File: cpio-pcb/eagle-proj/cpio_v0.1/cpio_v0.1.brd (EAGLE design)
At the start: 100 x 80 mm, 106 parts

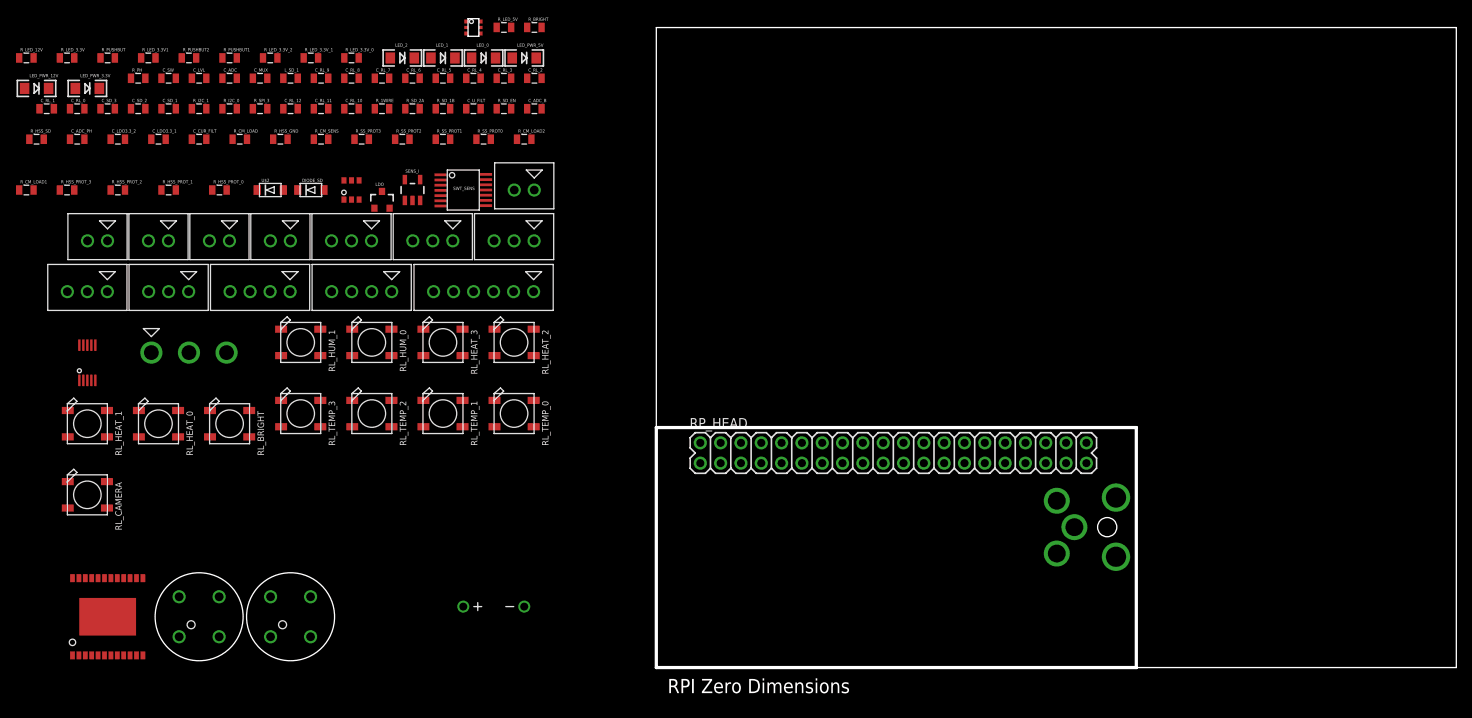
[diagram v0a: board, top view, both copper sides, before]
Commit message: scetch of PCB layout in order to see which components have to be removed
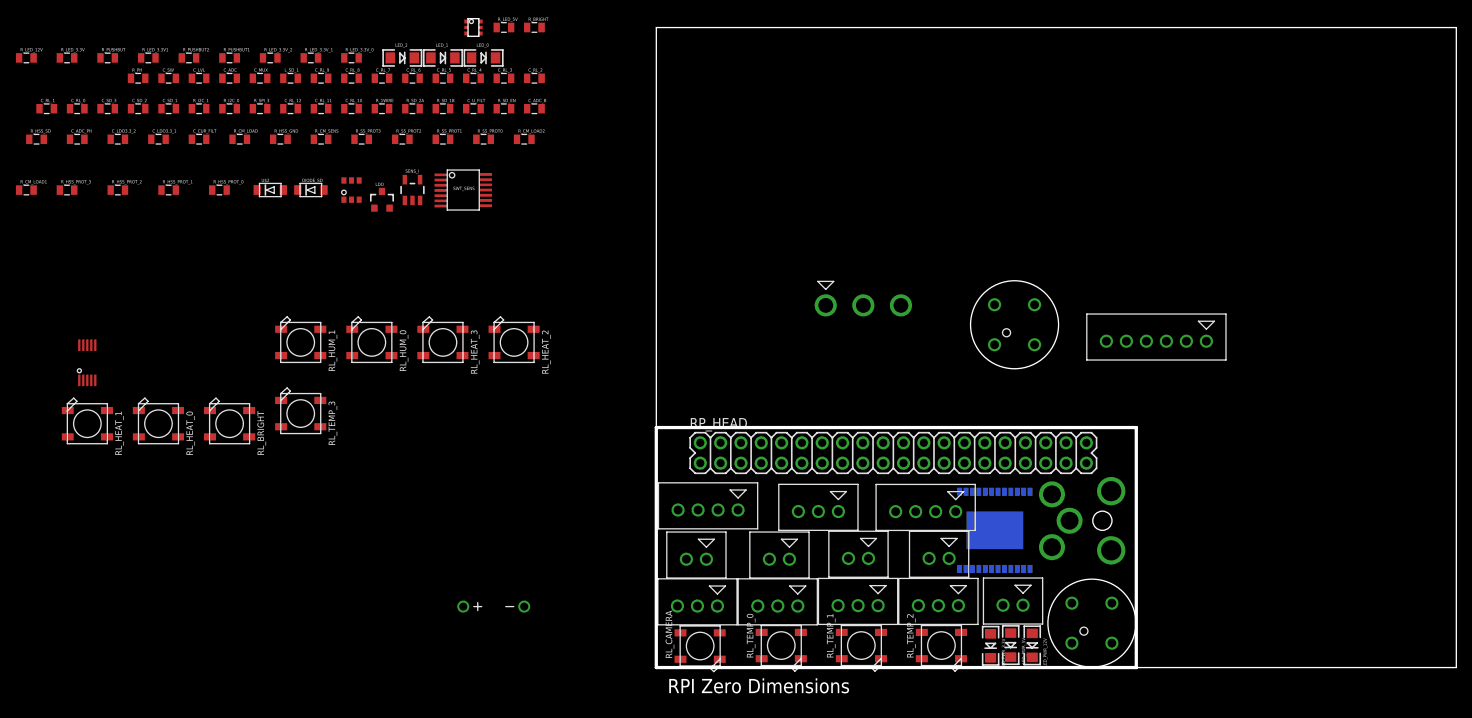
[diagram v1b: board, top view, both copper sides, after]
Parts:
- moved LED_PWR_12V 142.6 mm to (47.0, 2.77), turned to 270 degrees
- moved LED_PWR_3.3V 132.7 mm to (41.8, 2.72), turned to 270 degrees
- moved HEAT_3 112.4 mm to (35.4, 13.6)
- moved PUSH1 111.6 mm to (54.5, 5.55)
- moved SWT_HEAT 111.4 mm to (42.3, 17.1), flipped to the bottom
- moved PUSH 97.6 mm to (44.8, 42.9)
- moved HEAT_2 96.1 mm to (25.3, 13.6)
- moved LED_PWR_5V 95.3 mm to (44.3, 2.81), turned to 270 degrees
- moved SENS_TEMP_0 94.8 mm to (15.2, 7.69)
- moved SENS_HUM_1 87.6 mm to (33.7, 19.5)
- moved SWT_PWR 84.5 mm to (25.9, 45.3)
- moved CAMERA 84.3 mm to (62.5, 40.8)
- moved HEAT_1 80.5 mm to (15.4, 13.5)
- moved SENS_BRIGHT 80.2 mm to (44.6, 7.79)
- moved RL_CAMERA 78.9 mm to (5.48, 2.69), turned to 180 degrees
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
